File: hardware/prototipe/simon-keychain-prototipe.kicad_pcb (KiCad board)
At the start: 2 copper layers, 45.7 x 53.3 mm, 18 parts, among them J1 AVR-ISP-6, SW1 SW_Push, SW2 SW_Push, SW3 SW_Push, SW4 SW_Push, U1 ATtiny85-20PU

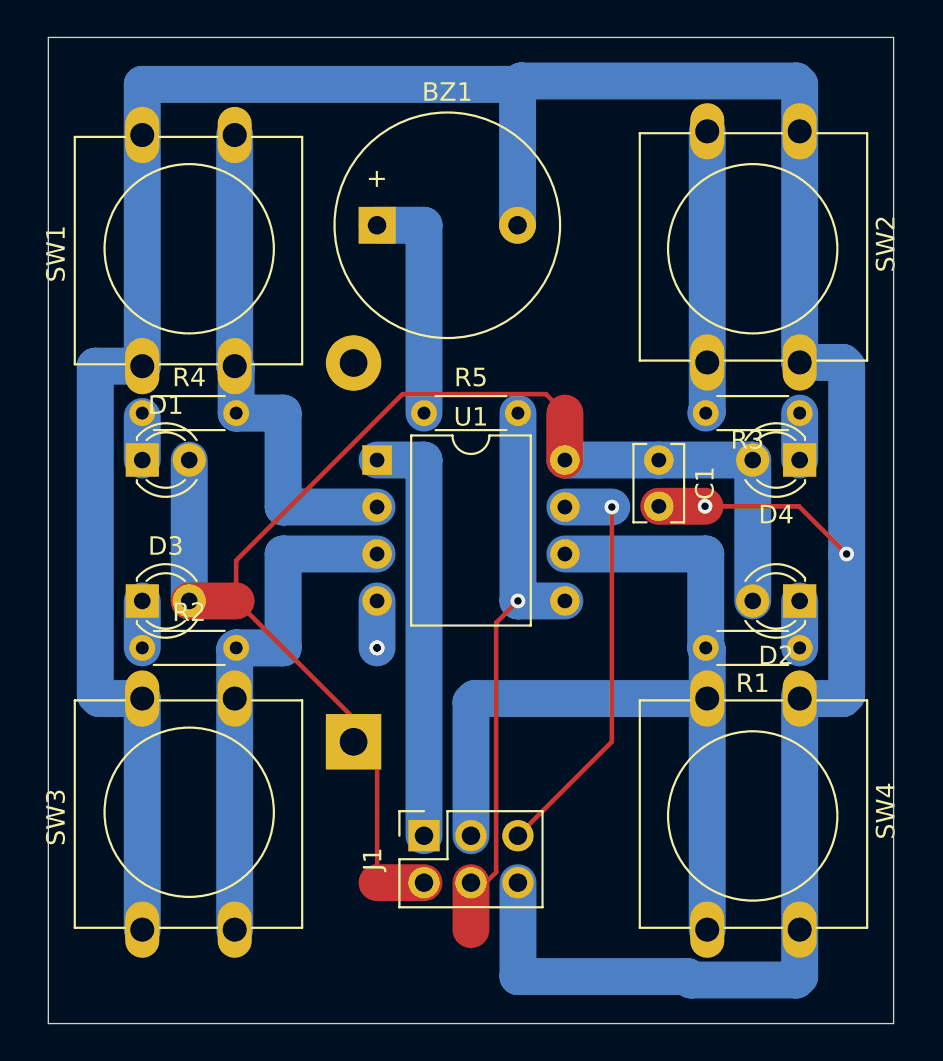
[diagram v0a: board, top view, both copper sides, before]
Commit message: Updated protoboard
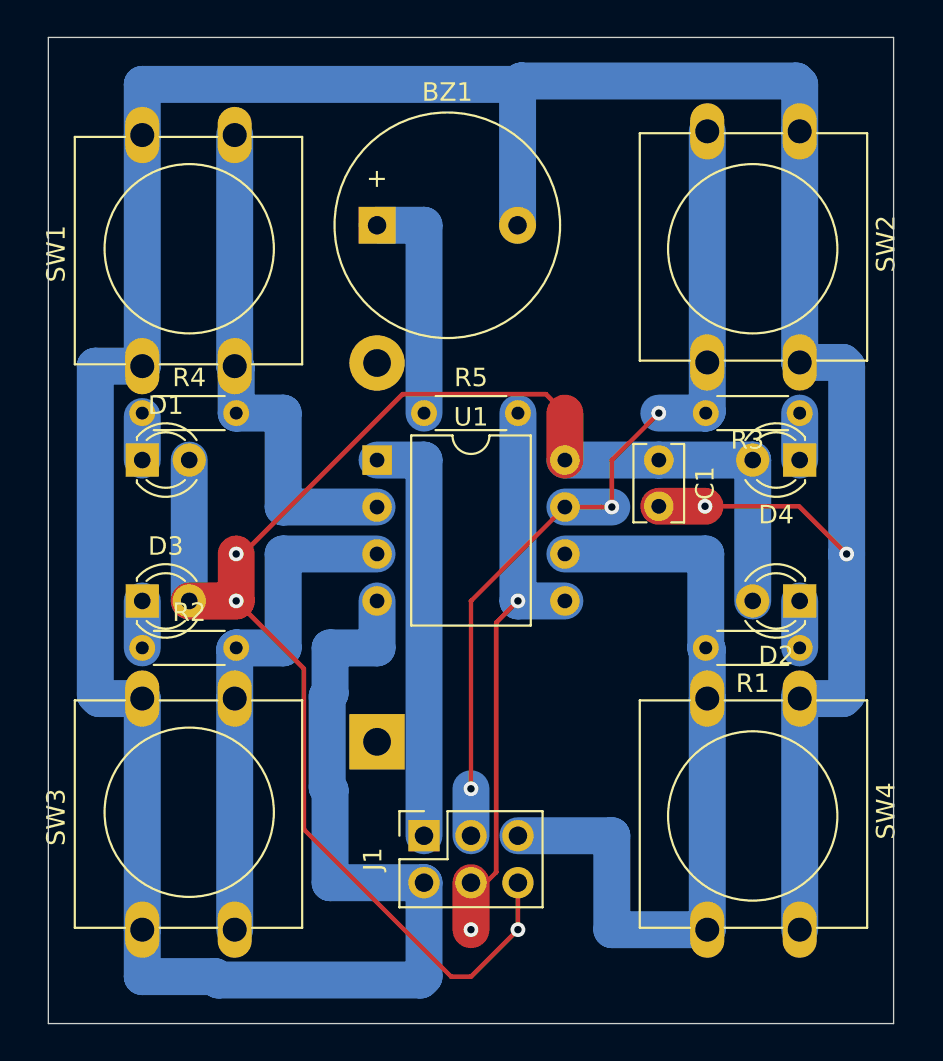
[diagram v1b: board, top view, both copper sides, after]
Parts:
- moved BT1 1.27 mm to (157.5, 109.2)
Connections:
- BT1 pad 1: +3V3 -> Net-(BT1-Pad1)
- J1 pad 2: +3V3 -> GND
- J1 pad 3: MISO -> SCK
- J1 pad 5: SCK -> MISO
- J1 pad 6: GND -> +3V3
- R3 pad 2: Net-(R3-Pad2) -> SCK
- SW2 pad 2: Net-(R3-Pad2) -> SCK
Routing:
- net SCK: track 22.4 -> 48.9 mm, vias 1 -> 3
- net GND: track 181.8 -> 202.3 mm, vias 4 -> 2
- net Net-(R3-Pad2): track 15.3 -> 0.00 mm
- net +3V3: track 75.5 -> 89.5 mm, vias 0 -> 3
- net MISO: track 48.1 -> 43.3 mm
- net MOSI: vias 1 -> 2
